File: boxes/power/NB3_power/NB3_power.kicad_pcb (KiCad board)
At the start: 2 copper layers, 71 parts, among them J1 Barrel_Jack_PJ-036AH-SMT-TR, J2 Conn_01x02_Male, J3 Conn_01x02_Male, J4 Conn_01x02_Male, J5 Conn_01x04_Male, J6 Conn_01x02_Male, J7 Conn_01x02_Male, SW1 SW_SPDT, SW2 SW_SPDT, U1 NiMH_Charger_LTC4010, U2 Voltage_Regulator_AP64501

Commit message: Work on NB3_power PCB
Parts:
- added H1: Standoff_SMT_5H_M2.5_9774050151R, NB3_power:Standoff_SMT_5H_M2.5_9774050151R, F.Cu at (109.0, 64.4)
- added H2: Standoff_SMT_5H_M2.5_9774050151R, NB3_power:Standoff_SMT_5H_M2.5_9774050151R, F.Cu at (188.0, 129.4)
- added H3: Standoff_SMT_5H_M2.5_9774050151R, NB3_power:Standoff_SMT_5H_M2.5_9774050151R, F.Cu at (188.0, 64.4)
- added H4: Standoff_SMT_5H_M2.5_9774050151R, NB3_power:Standoff_SMT_5H_M2.5_9774050151R, F.Cu at (109.0, 129.4)
- added Q1: Q_PMOS_GDS, NB3_power:PMOS_SMD_FDC658AP, F.Cu at (165.3, -64.6)
- added Q2: Q_NMOS_GDS, NB3_power:NMOS_SMD_SI3410DV-T1-GE3, F.Cu at (156.4, -50.6)
- XB1, XB10, XB11, XB12, XB2, XB3, XB4, XB5, XB6, XB7, XB8, XB9: moved to B.Cu
- moved SW1 263.6 mm to (162.6, -127.6)
- moved D6 260.6 mm to (207.3, -96.3)
- moved C13 260.4 mm to (164.1, -117.0)
- moved C10 258.2 mm to (162.5, -121.4)
- moved U2 258.2 mm to (171.6, -121.1)
- moved SW2 258.0 mm to (172.6, -127.6)
- moved C15 255.6 mm to (159.7, -117.0)
- moved R12 254.9 mm to (188.2, -117.0)
- moved R13 252.9 mm to (191.1, -117.0)
- moved F1 241.7 mm to (199.5, -89.0)
- moved R11 240.4 mm to (194.0, -117.0)
- moved C19 238.7 mm to (155.0, -117.1)
- moved F2 235.8 mm to (195.1, -86.0)
- moved R10 235.1 mm to (173.6, -116.9)
- moved C11 234.4 mm to (170.7, -116.9)
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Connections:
- net VIN renamed /VIN
- C10 pad 1: /VSYS_5V -> +5V
- C12 pad 1: /VSYS_5V -> +5V
- C5 pad 1: VBAT -> /VBAT
- C6 pad 1: /VSYS_5V -> +5V
- C7 pad 1: /VSYS_5V -> +5V
- C8 pad 1: /VSYS_5V -> +5V
- C9 pad 1: /VSYS_5V -> +5V
- F2 pad 2: 5V -> +5V
- F3 pad 2: 5V -> +5V
- F4 pad 2: 5V -> +5V
- F6 pad 2: 5V -> +5V
- L2 pad 2: /VSYS_5V -> +5V
- R11 pad 1: /VSYS_5V -> +5V
- R5 pad 1: VBAT -> /VBAT
- R8 pad 2: VBAT -> /VBAT
- SW1 pad 2: 5V -> +5V
- SW2 pad 2: 5V -> +5V
- U1 pad 10: VBAT -> /VBAT
- XB1 pad 1: VBAT -> /VBAT

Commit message: More work on NB3_power PCB
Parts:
- removed the D1 at (164.8, -60.8)
- removed the D2 at (170.3, -65.3)
- removed SW2: SW_SPDT, NB3_power:Switch_SPDT_SMD_Slide_JS102011JCQN
- added CR1: Schottky_PMEG3050EP,115, NB3_power:Schottky_PMEG3050EP,115, F.Cu at (134.6, 63.3)
- added CR2: Schottky_PMEG3050EP,115, NB3_power:Schottky_PMEG3050EP,115, F.Cu at (154.1, 44.4)
- added TH1: 10k, 3750, Resistor_SMD:R_0603_1608Metric, F.Cu at (209.0, -21.1)
- F1, F2, F4, F5, F6: value Polyfuse -> 1.1h2.2t
- F3: value Polyfuse -> 3h5t; footprint Fuse:Fuse_0805_2012Metric -> Fuse:Fuse_Bourns_MF-SM_7.98x5.44mm
- R8: value 40k -> 50k
- moved J4 263.0 mm to (147.6, 141.8)
- moved J6 247.4 mm to (120.5, 141.3)
- moved J2 221.0 mm to (181.1, 142.3)
- moved L2 204.3 mm to (139.6, 73.3)
- moved SW1 203.3 mm to (182.1, 74.8), turned to 90 degrees
- moved J5 187.2 mm to (182.1, 60.8)
- moved U2 182.9 mm to (148.6, 60.3)
- moved J3 174.1 mm to (182.1, 95.3)
- moved J7 156.3 mm to (122.5, 95.8)
- moved U1 149.1 mm to (135.1, 83.8)
- moved Q2 123.9 mm to (153.6, 73.3)
- moved F3 112.2 mm to (171.6, 64.3)
- moved J1 101.7 mm to (129.6, 73.8)
- moved H3 80.0 mm to (123.5, 111.8)
- moved H2 77.1 mm to (172.6, 53.8)
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- renumbered C5 to C2, C2 to C3, C3 to C5, D3 to D1, D4 to D2, D5 to D3, D6 to D4, R6 to R5, R5 to R6
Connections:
- C5 pad 1: Net-(C3-Pad1) (its old number) -> Net-(C4-Pad1)
- F1 pad 2: Net-(F1-Pad2) -> +5V
- F5 pad 2: Net-(F5-Pad2) -> +5V
- L1 pad 1: Net-(D2-Pad2) -> /VIN
- Q1 pad 2: Net-(D2-Pad2) -> /VIN
- Q2 pad 2: Net-(D2-Pad2) -> /VIN
- SW1 pad 1: Net-(F1-Pad2) -> /VIN
- SW1 pad 2: +5V -> Net-(SW1-Pad2)
- SW1 pad 3: Net-(SW1-Pad3) -> GND
- U1 pad 5: Net-(C3-Pad1) (its old number) -> Net-(C4-Pad1)
- U2 pad 3: /VIN -> Net-(SW1-Pad2)
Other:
- board outline added: 70 x 95 mm

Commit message: Work on NB3_power PCB (layout)
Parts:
- added C22: 10uF, Capacitor_SMD:C_0805_2012Metric, F.Cu at (184.1, 132.3)
- added C23: 10uF, Capacitor_SMD:C_0805_2012Metric, F.Cu at (174.6, 87.8)
- added C24: 10uF, Capacitor_SMD:C_0805_2012Metric, F.Cu at (147.6, 131.8)
- added C25: 10uF, Capacitor_SMD:C_0805_2012Metric, F.Cu at (111.5, 129.8)
- added C26: 10uF, Capacitor_SMD:C_0805_2012Metric, F.Cu at (121.5, 87.8)
- moved F1 225.4 mm to (183.1, 135.8), turned to 90 degrees
- moved F4 221.4 mm to (146.6, 136.3), turned to 90 degrees
- moved F5 211.2 mm to (110.5, 133.8), turned to 90 degrees
- moved R11 196.0 mm to (168.6, 77.3)
- moved C19 195.6 mm to (162.6, 78.3)
- moved C12 193.6 mm to (168.6, 75.8)
- moved C13 193.1 mm to (155.1, 75.8), turned to -90 degrees
- moved C15 193.0 mm to (152.6, 75.8), turned to -90 degrees
- moved R13 191.7 mm to (168.6, 73.3)
- moved R1 188.8 mm to (130.6, 70.8)
- moved C21 188.7 mm to (168.6, 71.8)
- moved R12 188.0 mm to (167.1, 69.8)
- moved R10 187.0 mm to (163.6, 69.8)
- moved C11 187.0 mm to (161.1, 69.8), turned to 180 degrees
- moved C10 186.4 mm to (177.6, 64.3), turned to -90 degrees
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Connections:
- XB1 pad 1: /VBAT -> GND
- XB1 pad MNT: /VBAT -> GND
- XB11 pad 1: GND -> /VBAT
- XB11 pad MNT: GND -> /VBAT
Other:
- board size 70 x 95 mm -> 80 x 97 mm

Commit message: More work on NB£_power PCB
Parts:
- added REF**: MountingHole_3.2mm_M3, MountingHole:MountingHole_3.2mm_M3, F.Cu at (184.1, 122.8)
- added REF**: MountingHole_3.2mm_M3, MountingHole:MountingHole_3.2mm_M3, F.Cu at (184.1, 52.8)
- added REF**: MountingHole_3.2mm_M3, MountingHole:MountingHole_3.2mm_M3, F.Cu at (112.0, 122.8)
- added REF**: MountingHole_3.2mm_M3, MountingHole:MountingHole_3.2mm_M3, F.Cu at (112.0, 52.8)
- J2, J3, J4, J6, J7: footprint Connector_PinHeader_2.54mm:PinHeader_1x02_P2.54mm_Vertical_SMD_Pin1Left -> Connector_PinHeader_2.54mm:PinHeader_1x02_P2.54mm_Vertical_SMD_Pin1Right
- J5: footprint Connector_PinHeader_2.54mm:PinHeader_1x04_P2.54mm_Vertical_SMD_Pin1Left -> Connector_PinHeader_2.54mm:PinHeader_1x04_P2.54mm_Vertical_SMD_Pin1Right
- L1: footprint Inductor_SMD:L_0805_2012Metric -> Inductor_SMD:L_Bourns_SRN6045TA
- Q1: value Q_PMOS_GDS -> PMOS
- Q2: value Q_NMOS_GDS -> NMOS
- moved D1 43.0 mm to (110.3, 102.8)
- moved D2 43.0 mm to (110.3, 100.8)
- moved D3 43.0 mm to (110.3, 98.8)
- moved D4 43.0 mm to (110.3, 104.8)
- moved R2 43.0 mm to (113.8, 102.8)
- moved R3 43.0 mm to (113.8, 100.8)
- moved R4 43.0 mm to (113.8, 98.8)
- moved R5 43.0 mm to (113.8, 104.8)
- moved L1 29.4 mm to (158.1, 100.8), turned to -90 degrees
- moved C2 29.0 mm to (164.1, 106.8), turned to 180 degrees
- moved Q2 27.0 mm to (147.1, 105.8), turned to -90 degrees
- moved R6 25.7 mm to (158.1, 108.4), turned to -90 degrees
- moved CR2 21.8 mm to (165.1, 100.8)
- moved C4 20.2 mm to (133.8, 105.8)
- moved C5 20.2 mm to (133.8, 107.8)
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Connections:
- L1 pad 1: /VIN -> /Drain
- Q1 pad 1: Net-(Q1-Pad1) -> /Drain
- Q1 pad 2: /VIN -> /Drain
- Q1 pad 3: /VIN -> Net-(Q1-Pad3)
- Q1 pad 4: (no net) -> /VIN
- Q1 pad 5: (no net) -> /Drain
- Q1 pad 6: (no net) -> /Drain
- Q2 pad 1: Net-(Q2-Pad1) -> /Drain
- Q2 pad 2: /VIN -> /Drain
- Q2 pad 3: GND -> Net-(Q2-Pad3)
- Q2 pad 4: (no net) -> GND
- Q2 pad 5: (no net) -> /Drain
- Q2 pad 6: (no net) -> /Drain
- U1 pad 12: Net-(Q2-Pad1) -> Net-(Q2-Pad3)
- U1 pad 14: Net-(Q1-Pad1) -> Net-(Q1-Pad3)
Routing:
- net Net-(XB7-Pad1): track 0.00 -> 49.0 mm
- net Net-(XB6-Pad1): track 0.00 -> 49.0 mm
- net Net-(XB3-Pad1): track 0.00 -> 49.0 mm
- net Net-(XB2-Pad1): track 0.00 -> 49.0 mm
- net Net-(XB10-Pad1): track 0.00 -> 49.0 mm
- net /VBAT: track 0.00 -> 12.9 mm
- net GND: track 0.00 -> 12.8 mm

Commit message: Still NB3_power PCB
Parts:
- C11: value 100n -> 100nF
- C3: value 0.1uF -> 100nF; footprint Capacitor_SMD:C_0603_1608Metric -> Capacitor_SMD:C_0402_1005Metric
- C4, C5: footprint Capacitor_SMD:C_0603_1608Metric -> Capacitor_SMD:C_0402_1005Metric
- L1: value 10uH -> SRN6045TA-6R3M
- R1, R2, R3, R4, R5, R7, R8, R9: footprint Resistor_SMD:R_0603_1608Metric -> Resistor_SMD:R_0402_1005Metric
- moved D1 41.5 mm to (110.0, 61.3)
- moved D2 41.5 mm to (110.0, 59.3)
- moved D3 41.5 mm to (110.0, 57.3)
- moved D4 41.5 mm to (110.0, 63.3)
- moved R2 41.5 mm to (113.5, 61.3)
- moved R3 41.5 mm to (113.5, 59.3)
- moved R4 41.5 mm to (113.5, 57.3)
- moved R5 41.5 mm to (113.5, 63.3)
- moved C2 28.9 mm to (135.3, 104.1), turned to 0 degrees
- moved CR2 27.0 mm to (142.3, 86.3), turned to 0 degrees
- moved R6 23.3 mm to (135.8, 101.6), turned to 0 degrees
- moved L1 15.9 mm to (142.3, 103.1), turned to 180 degrees
- moved R8 14.8 mm to (124.5, 98.8)
- moved R9 12.0 mm to (127.5, 101.3)
- moved C4 10.8 mm to (127.5, 97.1)
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
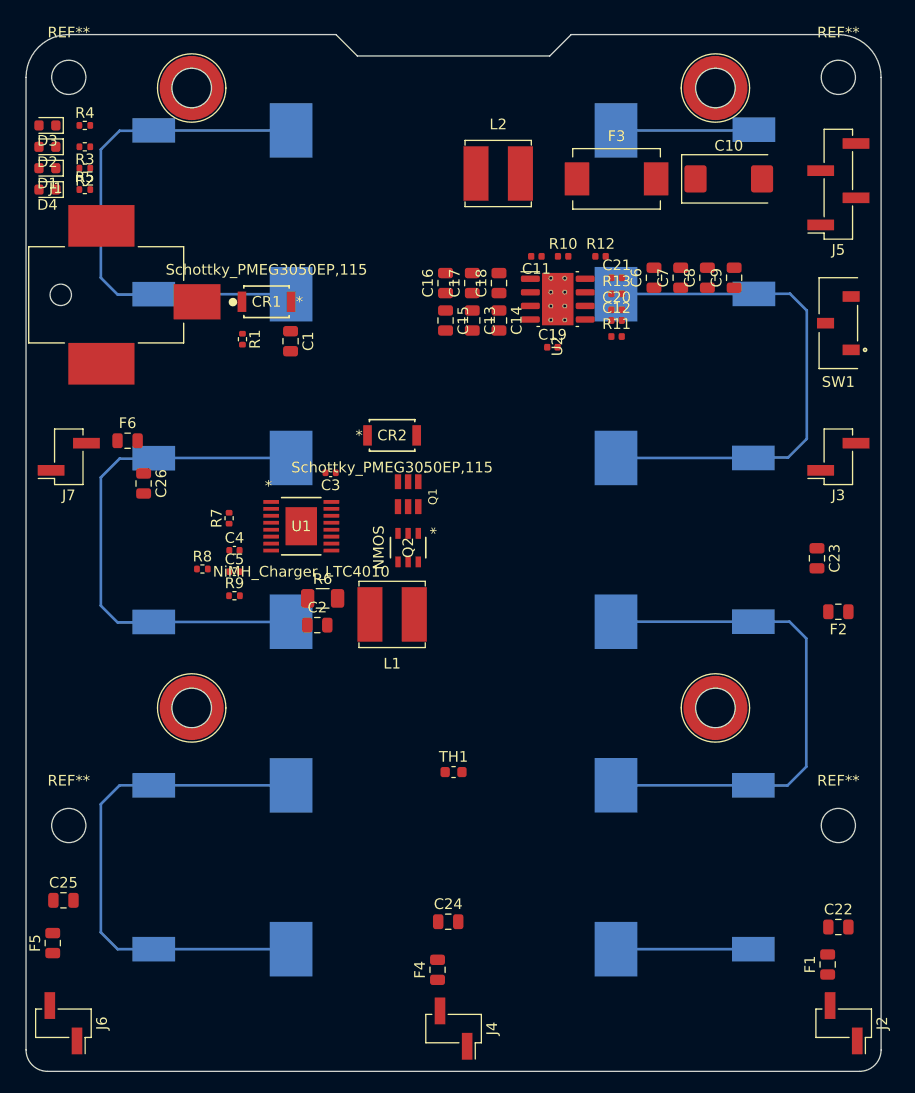
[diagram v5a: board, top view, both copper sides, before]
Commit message: NB3_power PCB layout finished
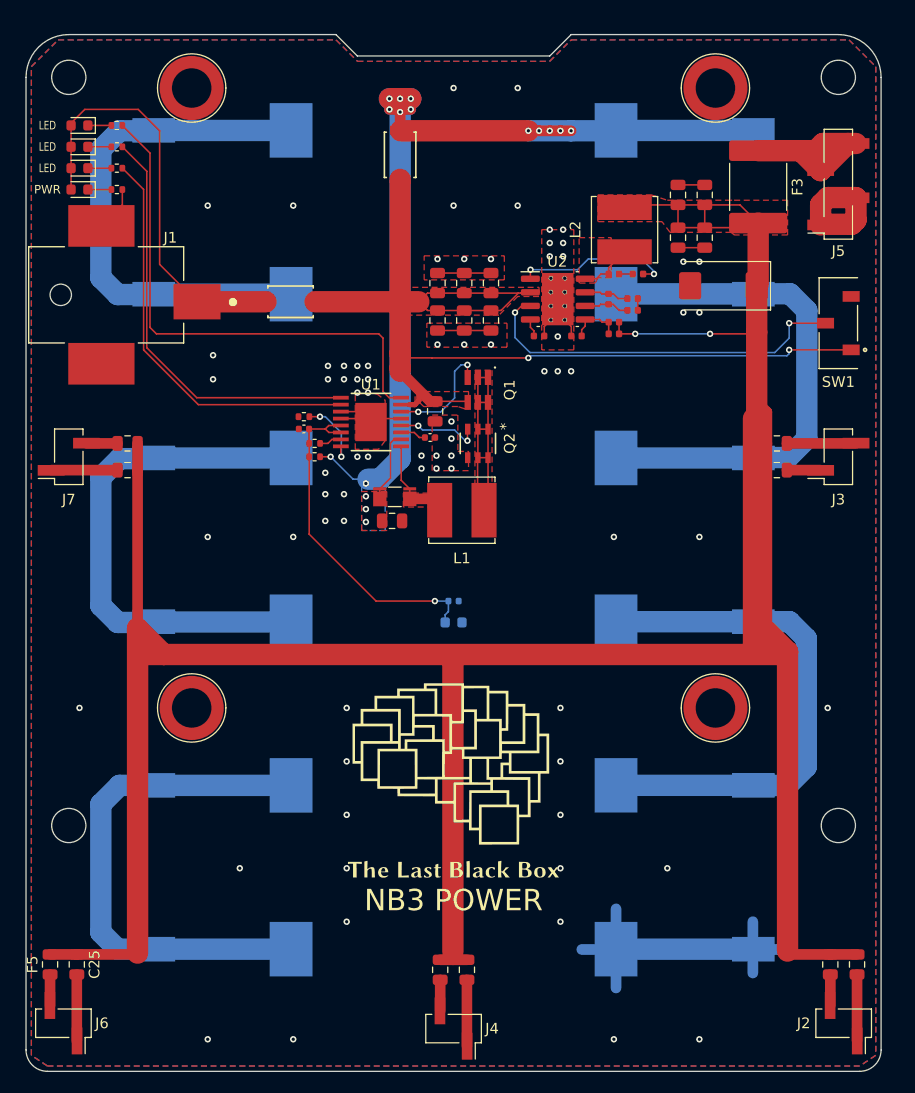
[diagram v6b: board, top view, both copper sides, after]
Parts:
- removed the R1 at (128.3, 77.3)
- added G***: LOGO, NB3_power:Logo_LBB_25mm, F.Cu at (148.1, 118.8)
- added G***: LOGO, NB3_power:Logo_VK_15mm, B.Cu at (148.1, 118.8)
- C5, TH1: moved to B.Cu
- F3: footprint Fuse:Fuse_Bourns_MF-SM_7.98x5.44mm -> Fuse:Fuse_2920_7451Metric
- moved CR2 26.3 mm to (143.1, 60.1), turned to 90 degrees
- moved C5 20.7 mm to (148.1, 101.8)
- moved F2 16.8 mm to (178.3, 87.1)
- moved R8 16.1 mm to (135.1, 87.1)
- moved C1 15.0 mm to (146.3, 84.1)
- moved R7 14.8 mm to (135.1, 88.3)
- moved TH1 14.0 mm to (148.1, 103.8)
- moved F3 13.3 mm to (176.6, 63.1), turned to -90 degrees
- moved C4 13.1 mm to (134.1, 85.7), turned to 180 degrees
- moved L2 12.9 mm to (164.1, 67.1), turned to 90 degrees
- moved C2 12.0 mm to (142.3, 94.3)
- moved R6 11.8 mm to (134.1, 84.6), turned to 180 degrees
- moved L1 11.7 mm to (148.8, 93.3)
- moved Q1 11.7 mm to (150.3, 82.1)
- moved Q2 11.7 mm to (150.3, 87.1)
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- renumbered R2 to R1, R11 to R10, R12 to R11, R13 to R12, R3 to R2, R4 to R3, R5 to R4, R6 to R5, R7 to R6, R8 to R7, R9 to R8, R10 to R9
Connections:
- J1 pad 3: Net-(J1-Pad3) -> GND
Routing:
- net +5V: track 0.00 -> 292.4 mm, vias 0 -> 2
- net /VIN: track 0.00 -> 103.4 mm, vias 0 -> 2
- net GND: track 12.8 -> 108.8 mm, vias 0 -> 75
- net /VBAT: track 12.9 -> 97.2 mm, vias 0 -> 16
- net Net-(R1-Pad2): track 0.00 -> 49.1 mm
- net Net-(R2-Pad2): track 0.00 -> 39.8 mm
- net +12V: track 0.00 -> 39.8 mm
- net Net-(R3-Pad2): track 0.00 -> 38.4 mm
- net Net-(SW1-Pad2): track 0.00 -> 35.4 mm, vias 0 -> 2
- net Net-(C4-Pad1): track 0.00 -> 32.3 mm, vias 0 -> 1
- net /Drain: track 0.00 -> 29.0 mm
- net Net-(F3-Pad1): track 0.00 -> 20.4 mm
- net Net-(C11-Pad2): track 0.00 -> 14.6 mm, vias 0 -> 2
- net Net-(Q1-Pad3): track 0.00 -> 10.7 mm, vias 0 -> 2
- net Net-(L1-Pad2): track 0.00 -> 8.49 mm
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- added copper zone on F.Cu, net +5V
- added copper zone on F.Cu, net /Drain
- added copper zone on B.Cu, net /VBAT
- added copper zone on F.Cu, net /VBAT
- added copper zone on F.Cu, net /VIN
- added copper zone on B.Cu, net GND
- added copper zone on F.Cu, net GND
- added copper zone on F.Cu, net Net-(L1-Pad2)
- added copper zone on F.Cu, net Net-(L2-Pad1)
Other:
- board text added: "LED"
- board text added: "NB3 POWER"
- board text added: "PWR"
